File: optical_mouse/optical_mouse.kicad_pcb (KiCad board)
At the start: 2 copper layers, 48.3 x 45.7 mm, 19 parts, among them Q1 CSTLS_G, U1 NANO

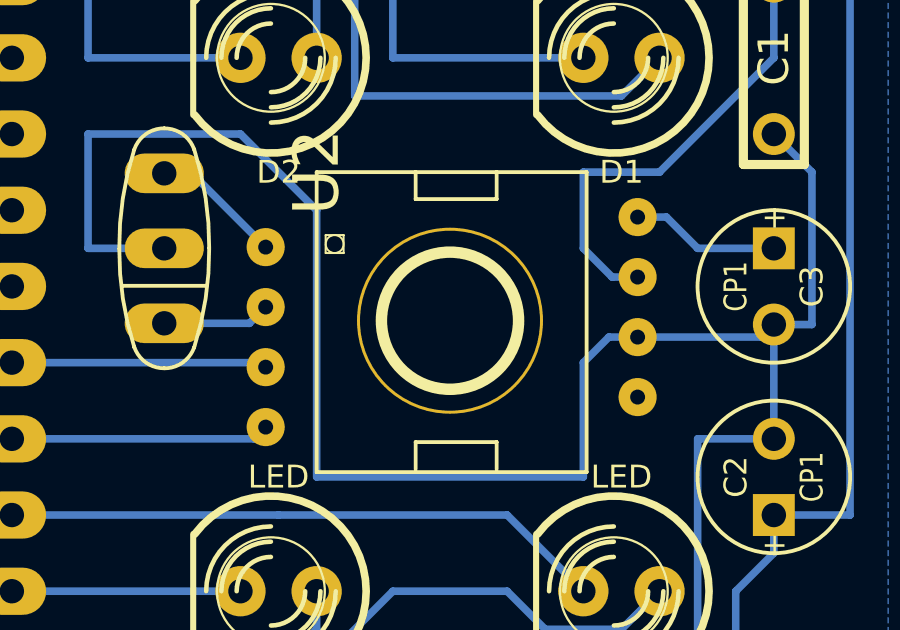
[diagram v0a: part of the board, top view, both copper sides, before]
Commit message: move camera hole into module
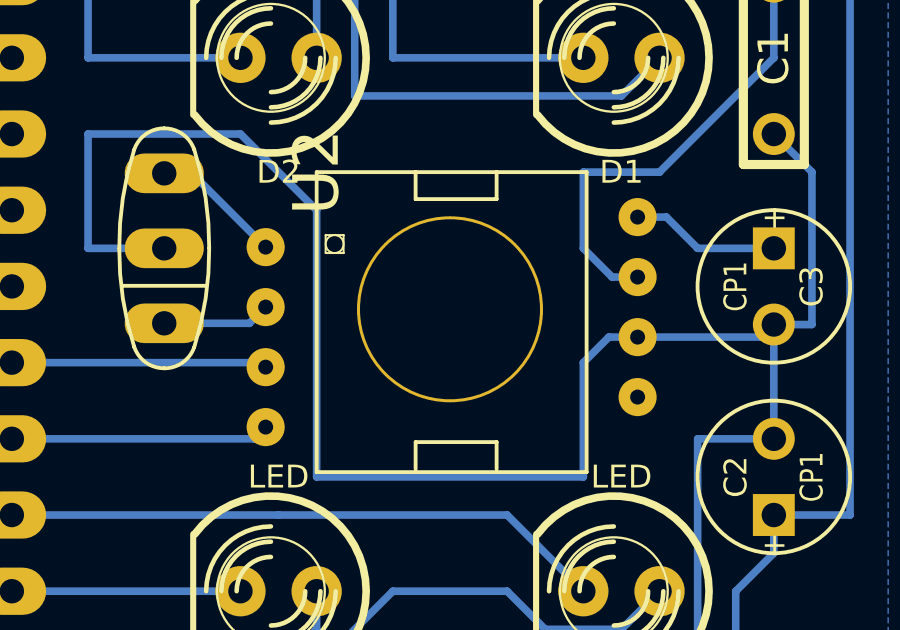
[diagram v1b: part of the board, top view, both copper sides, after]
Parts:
- removed the ? at (177.2, 126.9)
- Q1: value CSTLS_G -> (none)
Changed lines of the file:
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@@
     (tracks 93)
     (zones 0)
-    (modules 19)
+    (modules 18)
     (nets 16)
   )
@@
     (mod_text_size 1 1)
     (mod_text_width 0.15)
-    (pad_size 1.3208 2.6416)
-    (pad_drill 0.8128)
+    (pad_size 6.2 6.2)
+    (pad_drill 6)
     (pad_to_mask_clearance 0)
     (aux_axis_origin 0 0)
@@
       (effects (font (size 1.27 1.27) (thickness 0.0889)))
     )
-    (fp_text value CSTLS_G (at -0.18796 2.36474 90) (layer B.SilkS)
+    (fp_text value "" (at 0 3.175 90) (layer B.SilkS)
       (effects (font (size 1.27 1.27) (thickness 0.0889)))
     )
@@
       (net 11 N-0000034)
     )
+    (pad "" thru_hole circle (at 4.572 -4.445 270) (size 6.2 6.2) (drill 6)
+      (layers *.Cu *.Mask F.Paste F.SilkS)
+    )
   )
   (module R4 (layer F.Cu)
@@
     (fp_circle (center 0 0) (end 0 -2.286) (layer F.SilkS) (width 0.381))
     (pad "" thru_hole circle (at 0 0) (size 4.064 4.064) (drill 3.048)
-      (layers *.Cu *.Mask F.SilkS)
-    )
-  )
-  (module 1pin (layer F.Cu)
-    (at 177.165 126.873)
-    (descr "module 1 pin (ou trou mecanique de percage)")
-    (tags DEV)
-    (path 1pin)
-    (fp_text reference "" (at 0 -3.048) (layer F.SilkS)
-      (effects (font (size 1.016 1.016) (thickness 0.254)))
-    )
-    (fp_text value "" (at 0 2.794) (layer F.SilkS) hide
-      (effects (font (size 1.016 1.016) (thickness 0.254)))
-    )
-    (fp_circle (center 0 0) (end 0 -2.286) (layer F.SilkS) (width 0.381))
-    (pad "" thru_hole circle (at 0 0) (size 6.2 6.2) (drill 6)
       (layers *.Cu *.Mask F.SilkS)
     )
@@
   (segment (start 166.37 115.57) (end 172.72 115.57) (width 0.254) (layer B.Cu) (net 14))
   (segment (start 166.37 110.49) (end 166.37 115.57) (width 0.254) (layer B.Cu) (net 14))
-  (segment (start 167.64 142.24) (end 168.91 142.24) (width 0.254) (layer B.Cu) (net 15) (status 400000))
-  (segment (start 182.88 137.16) (end 184.15 135.89) (width 0.254) (layer B.Cu) (net 15) (status 800000))
+  (segment (start 167.64 142.24) (end 168.91 142.24) (width 0.254) (layer B.Cu) (net 15))
+  (segment (start 182.88 137.16) (end 184.15 135.89) (width 0.254) (layer B.Cu) (net 15))
   (segment (start 180.34 137.16) (end 182.88 137.16) (width 0.254) (layer B.Cu) (net 15))
   (segment (start 179.07 135.89) (end 180.34 137.16) (width 0.254) (layer B.Cu) (net 15))

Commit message: minor edits
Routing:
- net +5V: track 132.5 -> 131.0 mm
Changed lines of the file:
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@@
   (gr_line (start 193.04 105.41) (end 193.04 151.13) (angle 90) (layer Edge.Cuts) (width 0.1))
   (gr_line (start 144.78 105.41) (end 193.04 105.41) (angle 90) (layer Edge.Cuts) (width 0.1))
-  (segment (start 147.32 138.43) (end 151.13 138.43) (width 0.254) (layer B.Cu) (net 1))
-  (segment (start 177.8 107.95) (end 177.8 110.49) (width 0.254) (layer B.Cu) (net 1))
-  (segment (start 158.75 107.95) (end 177.8 107.95) (width 0.254) (layer B.Cu) (net 1))
-  (segment (start 158.75 130.81) (end 158.75 107.95) (width 0.254) (layer B.Cu) (net 1))
-  (segment (start 151.13 138.43) (end 158.75 130.81) (width 0.254) (layer B.Cu) (net 1))
+  (segment (start 147.32 138.43) (end 149.86 138.43) (width 0.254) (layer B.Cu) (net 1) (status 400000))
+  (segment (start 177.8 107.95) (end 177.8 110.49) (width 0.254) (layer B.Cu) (net 1) (status 800000))
+  (segment (start 160.02 107.95) (end 177.8 107.95) (width 0.254) (layer B.Cu) (net 1))
+  (segment (start 160.02 128.27) (end 160.02 107.95) (width 0.254) (layer B.Cu) (net 1))
+  (segment (start 149.86 138.43) (end 160.02 128.27) (width 0.254) (layer B.Cu) (net 1))
   (segment (start 182.56758 125.41758) (end 183.41848 125.41758) (width 0.254) (layer B.Cu) (net 1))
   (segment (start 181.61 124.46) (end 182.56758 125.41758) (width 0.254) (layer B.Cu) (net 1))

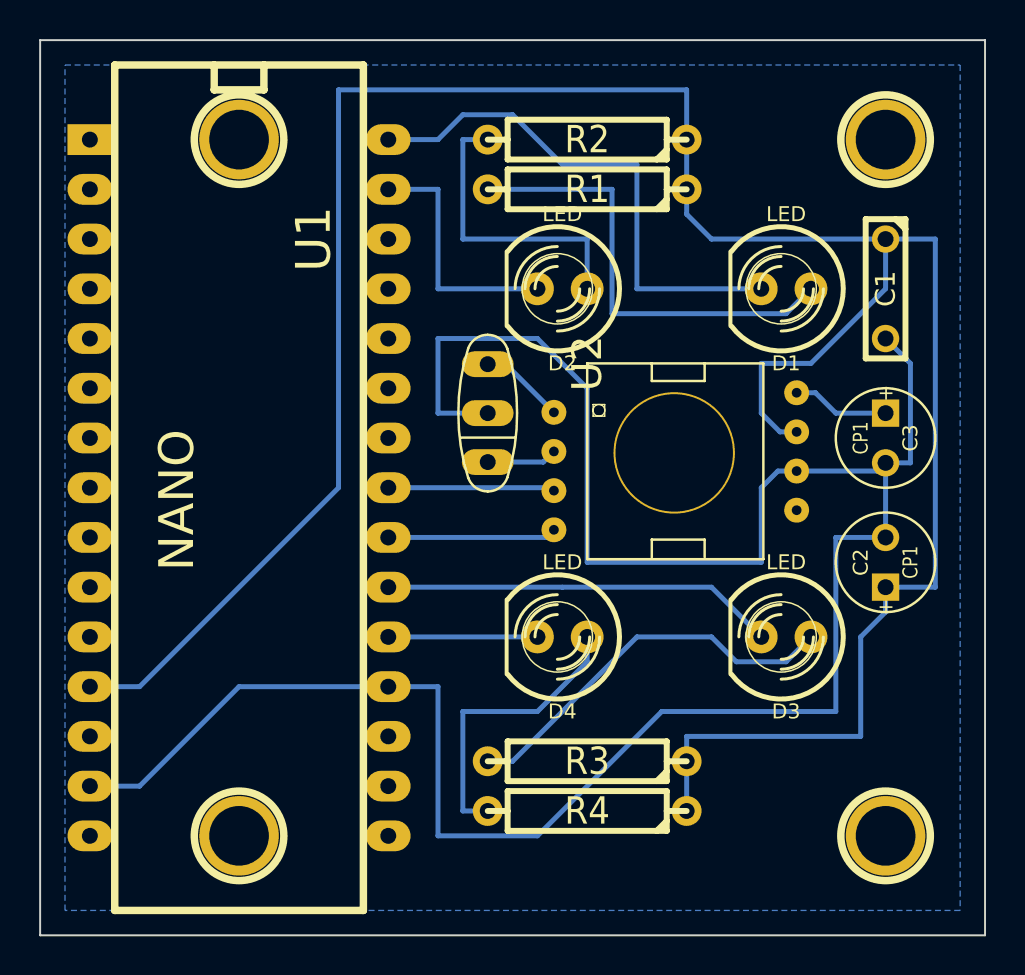
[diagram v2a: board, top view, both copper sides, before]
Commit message: changed track for more ground plane
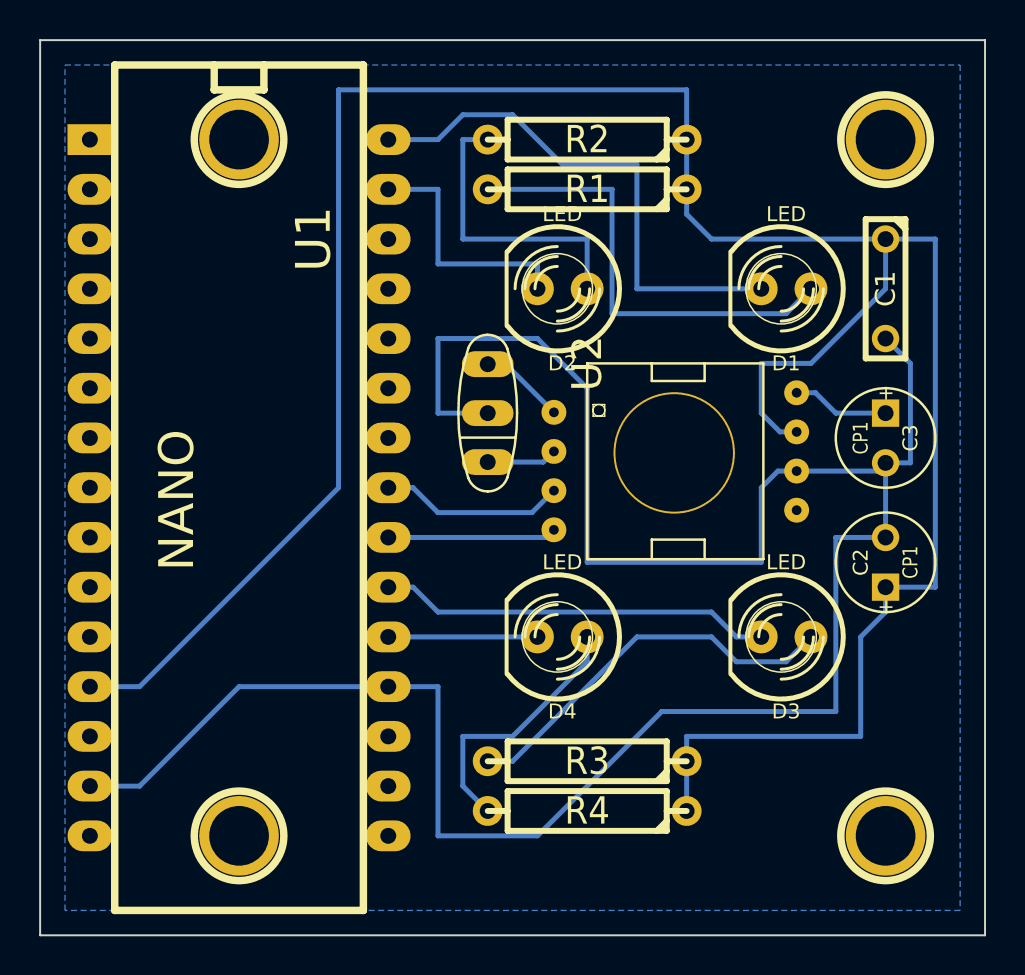
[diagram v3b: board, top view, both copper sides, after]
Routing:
- net N-000001: track 15.0 -> 13.5 mm
- net N-0000024: track 8.52 -> 9.45 mm
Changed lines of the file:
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@@
     (thickness 1.6)
     (drawings 4)
-    (tracks 93)
+    (tracks 98)
     (zones 0)
     (modules 18)
@@
   (gr_line (start 193.04 105.41) (end 193.04 151.13) (angle 90) (layer Edge.Cuts) (width 0.1))
   (gr_line (start 144.78 105.41) (end 193.04 105.41) (angle 90) (layer Edge.Cuts) (width 0.1))
-  (segment (start 147.32 138.43) (end 149.86 138.43) (width 0.254) (layer B.Cu) (net 1) (status 400000))
-  (segment (start 177.8 107.95) (end 177.8 110.49) (width 0.254) (layer B.Cu) (net 1) (status 800000))
+  (segment (start 147.32 138.43) (end 149.86 138.43) (width 0.254) (layer B.Cu) (net 1))
+  (segment (start 177.8 107.95) (end 177.8 110.49) (width 0.254) (layer B.Cu) (net 1))
   (segment (start 160.02 107.95) (end 177.8 107.95) (width 0.254) (layer B.Cu) (net 1))
   (segment (start 160.02 128.27) (end 160.02 107.95) (width 0.254) (layer B.Cu) (net 1))
@@
   (segment (start 165.1 120.65) (end 170.18 120.65) (width 0.254) (layer B.Cu) (net 2))
   (segment (start 165.1 124.46) (end 165.1 120.65) (width 0.254) (layer B.Cu) (net 2))
-  (segment (start 172.72 135.89) (end 172.72 137.16) (width 0.254) (layer B.Cu) (net 3))
-  (segment (start 166.37 144.78) (end 167.64 144.78) (width 0.254) (layer B.Cu) (net 3))
-  (segment (start 166.37 139.7) (end 166.37 144.78) (width 0.254) (layer B.Cu) (net 3))
-  (segment (start 170.18 139.7) (end 166.37 139.7) (width 0.254) (layer B.Cu) (net 3))
-  (segment (start 172.72 137.16) (end 170.18 139.7) (width 0.254) (layer B.Cu) (net 3))
-  (segment (start 162.56 133.35) (end 171.45 133.35) (width 0.254) (layer B.Cu) (net 4))
-  (segment (start 179.07 133.35) (end 181.61 135.89) (width 0.254) (layer B.Cu) (net 4))
-  (segment (start 171.45 133.35) (end 179.07 133.35) (width 0.254) (layer B.Cu) (net 4))
+  (segment (start 172.72 135.89) (end 172.72 137.16) (width 0.254) (layer B.Cu) (net 3) (status 400000))
+  (segment (start 166.37 143.51) (end 167.64 144.78) (width 0.254) (layer B.Cu) (net 3) (status 800000))
+  (segment (start 166.37 140.97) (end 166.37 143.51) (width 0.254) (layer B.Cu) (net 3))
+  (segment (start 168.91 140.97) (end 166.37 140.97) (width 0.254) (layer B.Cu) (net 3))
+  (segment (start 172.72 137.16) (end 168.91 140.97) (width 0.254) (layer B.Cu) (net 3))
+  (segment (start 162.56 133.35) (end 163.83 133.35) (width 0.254) (layer B.Cu) (net 4) (status 400000))
+  (segment (start 180.34 135.89) (end 181.61 135.89) (width 0.254) (layer B.Cu) (net 4) (status 800000))
+  (segment (start 179.07 134.62) (end 180.34 135.89) (width 0.254) (layer B.Cu) (net 4))
+  (segment (start 165.1 134.62) (end 179.07 134.62) (width 0.254) (layer B.Cu) (net 4))
+  (segment (start 163.83 133.35) (end 165.1 134.62) (width 0.254) (layer B.Cu) (net 4))
   (segment (start 162.56 135.89) (end 170.18 135.89) (width 0.254) (layer B.Cu) (net 5))
   (segment (start 162.56 110.49) (end 165.1 110.49) (width 0.254) (layer B.Cu) (net 6))
@@
   (segment (start 166.37 109.22) (end 168.91 109.22) (width 0.254) (layer B.Cu) (net 6))
   (segment (start 165.1 110.49) (end 166.37 109.22) (width 0.254) (layer B.Cu) (net 6))
-  (segment (start 162.56 130.81) (end 170.62958 130.81) (width 0.254) (layer B.Cu) (net 7))
-  (segment (start 170.62958 130.81) (end 171.02074 130.41884) (width 0.254) (layer B.Cu) (net 7))
-  (segment (start 162.56 128.27) (end 170.87088 128.27) (width 0.254) (layer B.Cu) (net 8))
-  (segment (start 170.87088 128.27) (end 171.02074 128.41986) (width 0.254) (layer B.Cu) (net 8))
+  (segment (start 162.56 130.81) (end 170.62958 130.81) (width 0.254) (layer B.Cu) (net 7) (status C00000))
+  (segment (start 170.62958 130.81) (end 171.02074 130.41884) (width 0.254) (layer B.Cu) (net 7) (status C00000))
+  (segment (start 162.56 128.27) (end 163.83 128.27) (width 0.254) (layer B.Cu) (net 8) (status 400000))
+  (segment (start 169.9006 129.54) (end 171.02074 128.41986) (width 0.254) (layer B.Cu) (net 8) (status 800000))
+  (segment (start 165.1 129.54) (end 169.9006 129.54) (width 0.254) (layer B.Cu) (net 8))
+  (segment (start 163.83 128.27) (end 165.1 129.54) (width 0.254) (layer B.Cu) (net 8))
   (segment (start 167.64 126.95936) (end 170.47972 126.95936) (width 0.254) (layer B.Cu) (net 9))
   (segment (start 170.47972 126.95936) (end 171.02074 126.41834) (width 0.254) (layer B.Cu) (net 9))
@@
   (segment (start 185.42 124.46) (end 187.96 124.46) (width 0.254) (layer B.Cu) (net 11))
   (segment (start 184.3786 123.4186) (end 185.42 124.46) (width 0.254) (layer B.Cu) (net 11))
-  (segment (start 162.56 113.03) (end 165.1 113.03) (width 0.254) (layer B.Cu) (net 12))
-  (segment (start 165.1 118.11) (end 170.18 118.11) (width 0.254) (layer B.Cu) (net 12))
-  (segment (start 165.1 113.03) (end 165.1 118.11) (width 0.254) (layer B.Cu) (net 12))
+  (segment (start 162.56 113.03) (end 165.1 113.03) (width 0.254) (layer B.Cu) (net 12) (status 400000))
+  (segment (start 170.18 116.84) (end 170.18 118.11) (width 0.254) (layer B.Cu) (net 12) (status 800000))
+  (segment (start 165.1 116.84) (end 170.18 116.84) (width 0.254) (layer B.Cu) (net 12))
+  (segment (start 165.1 113.03) (end 165.1 116.84) (width 0.254) (layer B.Cu) (net 12))
   (segment (start 167.64 113.03) (end 173.99 113.03) (width 0.254) (layer B.Cu) (net 13))
   (segment (start 182.88 119.38) (end 184.15 118.11) (width 0.254) (layer B.Cu) (net 13))
